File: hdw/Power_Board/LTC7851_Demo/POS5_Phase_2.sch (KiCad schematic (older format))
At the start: 23 parts, among them U301 LTC7851UHH, U501 SiC779

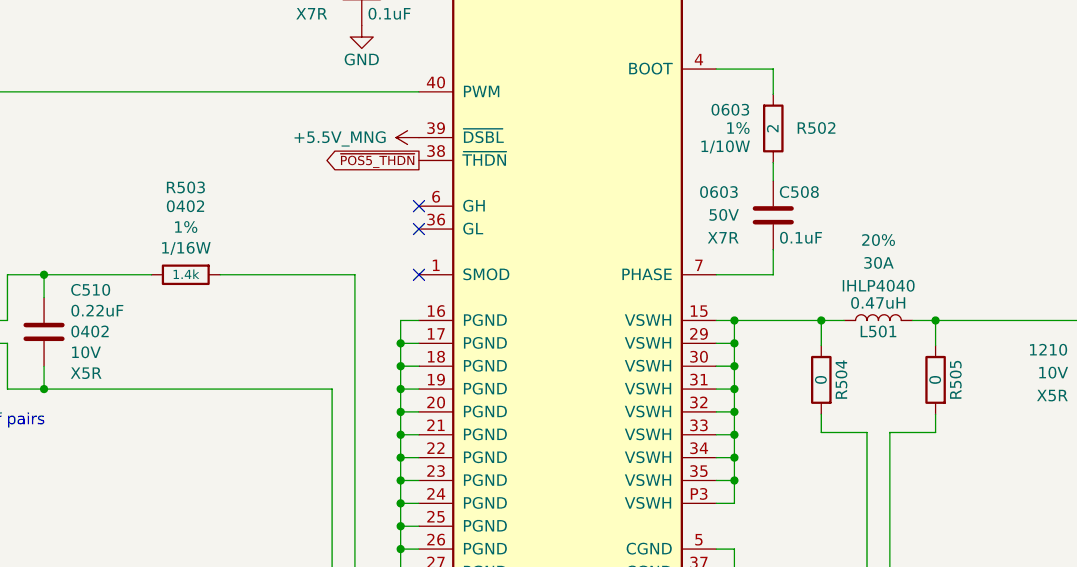
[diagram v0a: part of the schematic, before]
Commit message: Added changes to power board BOM
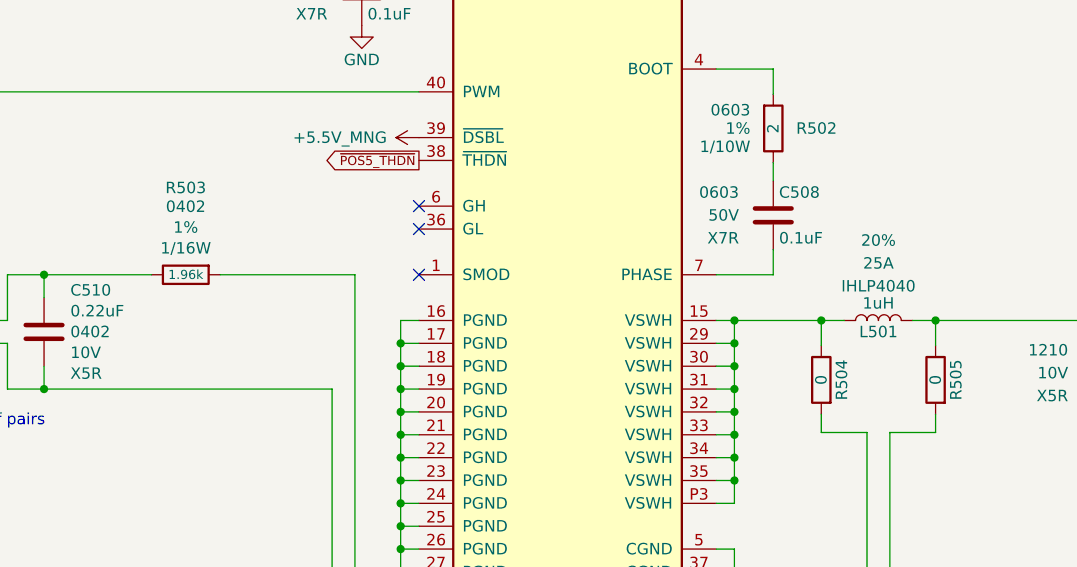
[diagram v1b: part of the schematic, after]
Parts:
- L501: value 0.47uH -> 1uH; Ampacity 30A -> 25A; Digi-Key PN 541-2595-1-ND -> 541-1306-1-ND
- R503: value 1.4k -> 1.96k; Digi-Key PN RMCF0402FT1K40CT-ND -> 311-1.96KLRCT-ND
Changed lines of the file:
@@
 AR Path="/5BB86F2C/5BD16C98" Ref="L501"  Part="1"
 F 0 "L501" V 7390 3310 50  0000 C CNN
-F 1 "0.47uH" V 7515 3310 50  0000 C CNN
+F 1 "1uH" V 7515 3310 50  0000 C CNN
 F 2 "Inductors_SMD:L_Vishay_IHLP-4040" H 7440 3310 50  0001 C CNN
 F 3 "" H 7440 3310 50  0001 C CNN
-F 4 "541-2595-1-ND" H 7440 3310 50  0001 C CNN "Digi-Key PN"
+F 4 "541-1306-1-ND" H 7440 3310 50  0001 C CNN "Digi-Key PN"
 F 5 "IHLP4040" V 7590 3310 50  0000 C CNN "display_footprint"
-F 6 "30A" V 7690 3310 50  0000 C CNN "Ampacity"
+F 6 "25A" V 7690 3310 50  0000 C CNN "Ampacity"
 F 7 "20%" V 7790 3310 50  0000 C CNN "Tolerance"
 	1    7440 3310
@@
 AR Path="/5BB86F2C/5BE651FC" Ref="R503"  Part="1"
 F 0 "R503" V 4790 3110 50  0000 C CNN
-F 1 "1.4k" V 4410 3110 40  0000 C CNN
+F 1 "1.96k" V 4410 3110 40  0000 C CNN
 F 2 "Resistors_SMD:R_0402" H 4410 3110 50  0001 C CNN
 F 3 "" H 4410 3110 50  0001 C CNN
-F 4 "RMCF0402FT1K40CT-ND" H 4710 3510 60  0001 C CNN "Digi-Key PN"
+F 4 "311-1.96KLRCT-ND" H 4710 3510 60  0001 C CNN "Digi-Key PN"
 F 5 "0402" V 4708 3110 50  0000 C CNN "display_footprint"
 F 6 "1%" V 4617 3110 50  0000 C CNN "Tolerance"

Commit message: Merging drews_branch_3 into master
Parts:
- C501, C502, C503, C505, C507, C515: symbol Custom_Library:CP_Tant_Custom -> LED_Display_Local_Library:CP_Tant_Custom
- C504, C506, C508, C509, C510, C511, C512, C513, C514: symbol Custom_Library:C_Custom -> LED_Display_Local_Library:C_Custom
- L501: symbol Custom_Library:L_Custom -> LED_Display_Local_Library:L_Custom
- R501, R502, R503, R504, R505: symbol Custom_Library:R_Custom -> LED_Display_Local_Library:R_Custom
- U301: symbol Custom_Library:LTC7851UHH -> LED_Display_Local_Library:LTC7851UHH
- U501: symbol Custom_Library:SiC779 -> LED_Display_Local_Library:SiC779
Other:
- note added: "05. +5V Phase 2"
- note removed: "+5V Phase 2"
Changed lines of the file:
@@
 POS5_PGOOD_OC
 $Comp
-L Custom_Library:C_Custom C?
+L LED_Display_Local_Library:C_Custom C?
 U 1 1 5BD16C10
 P 4560 1340
@@
 F 2 "Capacitors_SMD:C_0603_HandSoldering" H 4598 1190 50  0001 C CNN
 F 3 "" H 4585 1440 50  0001 C CNN
-F 4 "0603" H 4410 1440 50  0000 R CNN "display_footprint"
-F 5 "16V" H 4410 1340 50  0000 R CNN "Voltage"
-F 6 "X7R" H 4410 1240 50  0000 R CNN "Dielectric"
-F 7 "1276-6524-1-ND" H 4985 1840 60  0001 C CNN "Digi-Key PN"
+F 4 "1276-6524-1-ND" H 4985 1840 60  0001 C CNN "Digi-Key PN"
+F 5 "0603" H 4410 1440 50  0000 R CNN "display_footprint"
+F 6 "16V" H 4410 1340 50  0000 R CNN "Voltage"
+F 7 "X7R" H 4410 1240 50  0000 R CNN "Dielectric"
 	1    4560 1340
 	1    0    0    -1
@@
 $EndComp
 $Comp
-L Custom_Library:SiC779 U?
+L LED_Display_Local_Library:SiC779 U?
 U 1 1 5BD16C1E
 P 6080 2810
@@
 	6810 3910 6810 4010
 $Comp
-L Custom_Library:L_Custom L?
+L LED_Display_Local_Library:L_Custom L?
 U 1 1 5BD16C98
 P 7440 3310
@@
 	6810 1710 6810 1810
 $Comp
-L Custom_Library:R_Custom R?
+L LED_Display_Local_Library:R_Custom R?
 U 1 1 5BD16CB9
 P 6980 2470
@@
 $EndComp
 $Comp
-L Custom_Library:C_Custom C?
+L LED_Display_Local_Library:C_Custom C?
 U 1 1 5BD16CC4
 P 6980 2850
@@
 F 2 "Capacitors_SMD:C_0603" H 7018 2700 50  0001 C CNN
 F 3 "" H 7005 2950 50  0001 C CNN
-F 4 "0603" H 6830 2950 50  0000 R CNN "display_footprint"
-F 5 "50V" H 6830 2850 50  0000 R CNN "Voltage"
-F 6 "X7R" H 6830 2750 50  0000 R CNN "Dielectric"
-F 7 "490-4779-1-ND" H 7405 3350 60  0001 C CNN "Digi-Key PN"
+F 4 "490-4779-1-ND" H 7405 3350 60  0001 C CNN "Digi-Key PN"
+F 5 "0603" H 6830 2950 50  0000 R CNN "display_footprint"
+F 6 "50V" H 6830 2850 50  0000 R CNN "Voltage"
+F 7 "X7R" H 6830 2750 50  0000 R CNN "Dielectric"
 	1    6980 2850
 	1    0    0    -1
@@
 Connection ~ 6810 3310
 $Comp
-L Custom_Library:C_Custom C?
+L LED_Display_Local_Library:C_Custom C?
 U 1 1 5BD16CFA
 P 7880 1340
@@
 	8480 1110 7880 1110
 $Comp
-L Custom_Library:C_Custom C?
+L LED_Display_Local_Library:C_Custom C?
 U 1 1 5BD16D21
 P 8420 3540
@@
 F 2 "Capacitors_SMD:C_1210" H 8458 3390 50  0001 C CNN
 F 3 "" H 8445 3640 50  0001 C CNN
-F 4 "1210" H 8270 3640 50  0000 R CNN "display_footprint"
-F 5 "10V" H 8270 3540 50  0000 R CNN "Voltage"
-F 6 "X5R" H 8270 3440 50  0000 R CNN "Dielectric"
-F 7 "587-3432-1-ND" H 8845 4040 60  0001 C CNN "Digi-Key PN"
+F 4 "587-3432-1-ND" H 8845 4040 60  0001 C CNN "Digi-Key PN"
+F 5 "1210" H 8270 3640 50  0000 R CNN "display_footprint"
+F 6 "10V" H 8270 3540 50  0000 R CNN "Voltage"
+F 7 "X5R" H 8270 3440 50  0000 R CNN "Dielectric"
 	1    8420 3540
 	1    0    0    -1
@@
 $EndComp
 $Comp
-L Custom_Library:LTC7851UHH U?
+L LED_Display_Local_Library:LTC7851UHH U?
 U 3 1 5BD16D95
 P 2510 4210
@@
 $EndComp
 $Comp
-L Custom_Library:C_Custom C?
+L LED_Display_Local_Library:C_Custom C?
 U 1 1 5BD16DE2
 P 5180 1870
@@
 F 2 "Capacitors_SMD:C_0603" H 5218 1720 50  0001 C CNN
 F 3 "" H 5205 1970 50  0001 C CNN
-F 4 "0603" H 5030 1970 50  0000 R CNN "display_footprint"
-F 5 "50V" H 5030 1870 50  0000 R CNN "Voltage"
-F 6 "X7R" H 5030 1770 50  0000 R CNN "Dielectric"
-F 7 "490-4779-1-ND" H 5605 2370 60  0001 C CNN "Digi-Key PN"
+F 4 "490-4779-1-ND" H 5605 2370 60  0001 C CNN "Digi-Key PN"
+F 5 "0603" H 5030 1970 50  0000 R CNN "display_footprint"
+F 6 "50V" H 5030 1870 50  0000 R CNN "Voltage"
+F 7 "X7R" H 5030 1770 50  0000 R CNN "Dielectric"
 	1    5180 1870
 	1    0    0    -1
 $EndComp
 $Comp
-L Custom_Library:R_Custom R?
+L LED_Display_Local_Library:R_Custom R?
 U 1 1 5BD16DED
 P 5180 1340
@@
 	8480 1030 8480 1110
 $Comp
-L Custom_Library:C_Custom C?
+L LED_Display_Local_Library:C_Custom C?
 U 1 1 5BD16E10
 P 7280 1340
@@
 F 2 "Capacitors_SMD:C_0603" H 7318 1190 50  0001 C CNN
 F 3 "" H 7305 1440 50  0001 C CNN
-F 4 "0603" H 7130 1440 50  0000 R CNN "display_footprint"
-F 5 "16V" H 7130 1340 50  0000 R CNN "Voltage"
-F 6 "X7R" H 7130 1240 50  0000 R CNN "Dielectric"
-F 7 "1276-6524-1-ND" H 7705 1840 60  0001 C CNN "Digi-Key PN"
+F 4 "1276-6524-1-ND" H 7705 1840 60  0001 C CNN "Digi-Key PN"
+F 5 "0603" H 7130 1440 50  0000 R CNN "display_footprint"
+F 6 "16V" H 7130 1340 50  0000 R CNN "Voltage"
+F 7 "X7R" H 7130 1240 50  0000 R CNN "Dielectric"
 	1    7280 1340
 	1    0    0    -1
@@
 Connection ~ 9020 3310
 $Comp
-L Custom_Library:CP_Tant_Custom C?
+L LED_Display_Local_Library:CP_Tant_Custom C?
 U 1 1 5BD16E1C
 P 9620 3540
@@
 $EndComp
 $Comp
-L Custom_Library:C_Custom C?
+L LED_Display_Local_Library:C_Custom C?
 U 1 1 5BD16E4F
 P 9020 3540
@@
 $EndComp
 $Comp
-L Custom_Library:C_Custom C?
+L LED_Display_Local_Library:C_Custom C?
 U 1 1 5BD16E5B
 P 8480 1340
@@
 $EndComp
 $Comp
-L Custom_Library:CP_Tant_Custom C?
+L LED_Display_Local_Library:CP_Tant_Custom C?
 U 1 1 5BD16E66
 P 3330 7370
@@
 $EndComp
 $Comp
-L Custom_Library:CP_Tant_Custom C?
+L LED_Display_Local_Library:CP_Tant_Custom C?
 U 1 1 5BD16E71
 P 3930 7370
@@
 $EndComp
 $Comp
-L Custom_Library:CP_Tant_Custom C?
+L LED_Display_Local_Library:CP_Tant_Custom C?
 U 1 1 5BD16E7C
 P 4530 7370
@@
 $EndComp
 $Comp
-L Custom_Library:CP_Tant_Custom C?
+L LED_Display_Local_Library:CP_Tant_Custom C?
 U 1 1 5BD16E87
 P 5130 7370
@@
 $EndComp
 $Comp
-L Custom_Library:CP_Tant_Custom C?
+L LED_Display_Local_Library:CP_Tant_Custom C?
 U 1 1 5BD16E92
 P 5730 7370
@@
 Connection ~ 6810 4010
 Text Notes 540  690  0    100  ~ 20
-+5V Phase 2
+05. +5V Phase 2
 NoConn ~ 5430 2810
 NoConn ~ 5430 2910
@@
 	7590 3310 7690 3310
 $Comp
-L Custom_Library:R_Custom R?
+L LED_Display_Local_Library:R_Custom R?
 U 1 1 5BE651FC
 P 4410 3110
@@
 $EndComp
 $Comp
-L Custom_Library:C_Custom C?
+L LED_Display_Local_Library:C_Custom C?
 U 1 1 5BE65207
 P 3790 3360
@@
 	7190 3310 7190 3420
 $Comp
-L Custom_Library:R_Custom R?
+L LED_Display_Local_Library:R_Custom R?
 U 1 1 5BE65227
 P 7190 3570
@@
 $EndComp
 $Comp
-L Custom_Library:R_Custom R?
+L LED_Display_Local_Library:R_Custom R?
 U 1 1 5BE65232
 P 7690 3570
@@
 Wire Wire Line
 	7690 3310 8420 3310
+$Comp
+L LED_Display_Local_Library:MU_Logo #G?
+U 1 1 5C003CA7
+P 9900 1100
+F 0 "#G?" H 9900 614 60  0001 C CNN
+F 1 "MU_Logo" H 9900 1586 60  0001 C CNN
+F 2 "" H 9900 1100 50  0001 C CNN
+F 3 "" H 9900 1100 50  0001 C CNN
+	1    9900 1100
+	1    0    0    -1
+$EndComp
 $EndSCHEMATC

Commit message: Schematic cleanup
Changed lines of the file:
@@
 Date "2018-11-28"
 Rev "A"
-Comp "Marquette Senior Design 2018, Group E44"
+Comp "Marquette University Senior Design 2018 Group E44"
 Comment1 ""
 Comment2 ""
@@
 AR Path="/5BB86F29/5BD16CB9" Ref="R?"  Part="1"
 AR Path="/5BB86F2C/5BD16CB9" Ref="R502"  Part="1"
-F 0 "R502" H 6880 2470 50  0000 R CNN
+F 0 "R502" H 6920 2470 50  0000 R CNN
 F 1 "2" V 6980 2470 50  0000 C CNN
 F 2 "Resistors_SMD:R_0603" H 6980 2470 50  0001 C CNN
@@
 AR Path="/5BB86F29/5BD16DED" Ref="R?"  Part="1"
 AR Path="/5BB86F2C/5BD16DED" Ref="R501"  Part="1"
-F 0 "R501" H 5080 1340 50  0000 R CNN
+F 0 "R501" H 5120 1340 50  0000 R CNN
 F 1 "2" V 5180 1340 50  0000 C CNN
 F 2 "Resistors_SMD:R_0603" H 5180 1340 50  0001 C CNN
@@
 AR Path="/5BB86F29/5BE65227" Ref="R?"  Part="1"
 AR Path="/5BB86F2C/5BE65227" Ref="R504"  Part="1"
-F 0 "R504" V 7280 3570 50  0000 C CNN
+F 0 "R504" H 7240 3570 50  0000 L CNN
 F 1 "0" V 7190 3570 50  0000 C CNN
 F 2 "Resistors_SMD:R_0402" H 7190 3570 50  0001 C CNN
@@
 AR Path="/5BB86F29/5BE65232" Ref="R?"  Part="1"
 AR Path="/5BB86F2C/5BE65232" Ref="R505"  Part="1"
-F 0 "R505" V 7780 3570 50  0000 C CNN
+F 0 "R505" H 7740 3570 50  0000 L CNN
 F 1 "0" V 7690 3570 50  0000 C CNN
 F 2 "Resistors_SMD:R_0402" H 7690 3570 50  0001 C CNN
